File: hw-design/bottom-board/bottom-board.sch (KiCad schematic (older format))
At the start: 0 parts

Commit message: bottom,sch: minor adjustments
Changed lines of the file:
@@
 F1 "connectors.sch" 60
 $EndSheet
-Text Notes 1350 5600 0    80   ~ 0
+Text Notes 1350 6000 0    80   ~ 0
 - All resistors named as RA* must have 1% tolerance\n- All non-polarized capacitors named as CA* must use NP0 Temp. Coef.\n- All other non-polarized capacitors should use X7R Temp. Coef.\n- Decoupling caps must be placed as close as possible of the IC power pins
-Text Notes 1300 5000 0    100  ~ 20
+Text Notes 1300 5400 0    100  ~ 20
 Notes\n
 Wire Notes Line
-	1200 5000 1200 6200
+	1200 5400 1200 6600
 Wire Notes Line
-	1200 6200 6850 6200
+	1200 6600 6850 6600
 Wire Notes Line
-	6850 6200 6850 4800
+	6850 6600 6850 5200
 Wire Notes Line
-	6850 4800 1200 4800
+	6850 5200 1200 5200
 Wire Notes Line
-	1200 4800 1200 5050
+	1200 5200 1200 5450
 Wire Notes Line
-	1200 5050 6850 5050
+	1200 5450 6850 5450
 $Sheet
 S 1300 2250 2150 400

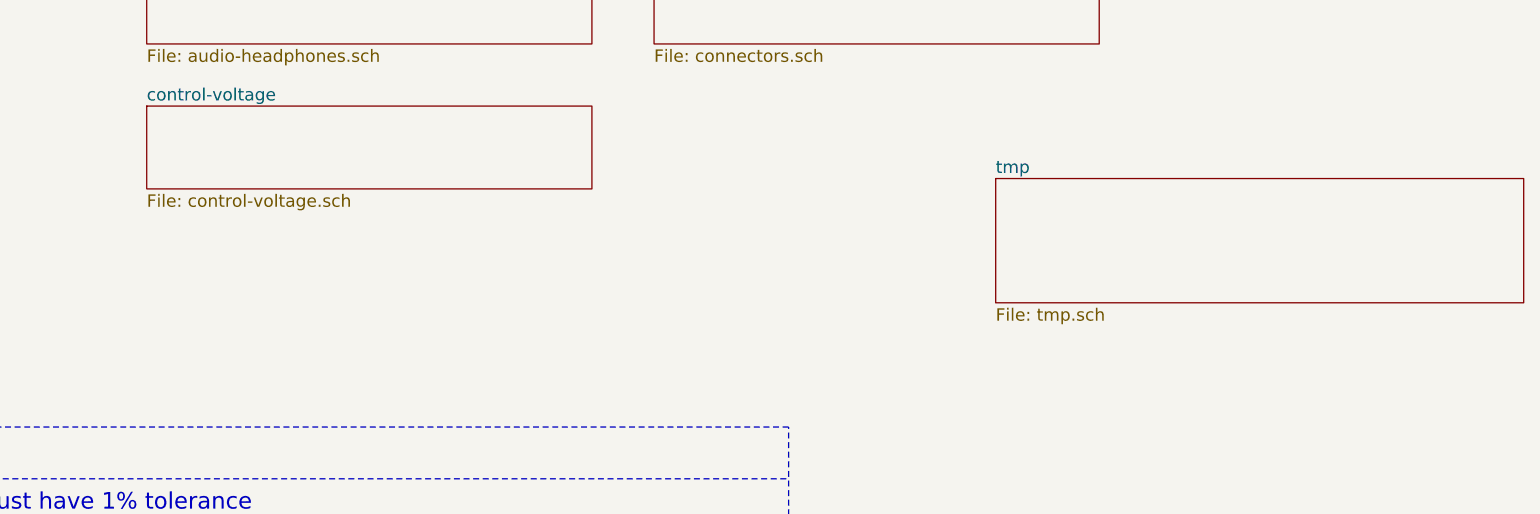
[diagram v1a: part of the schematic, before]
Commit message: bottom,sch: initial spdif circuit
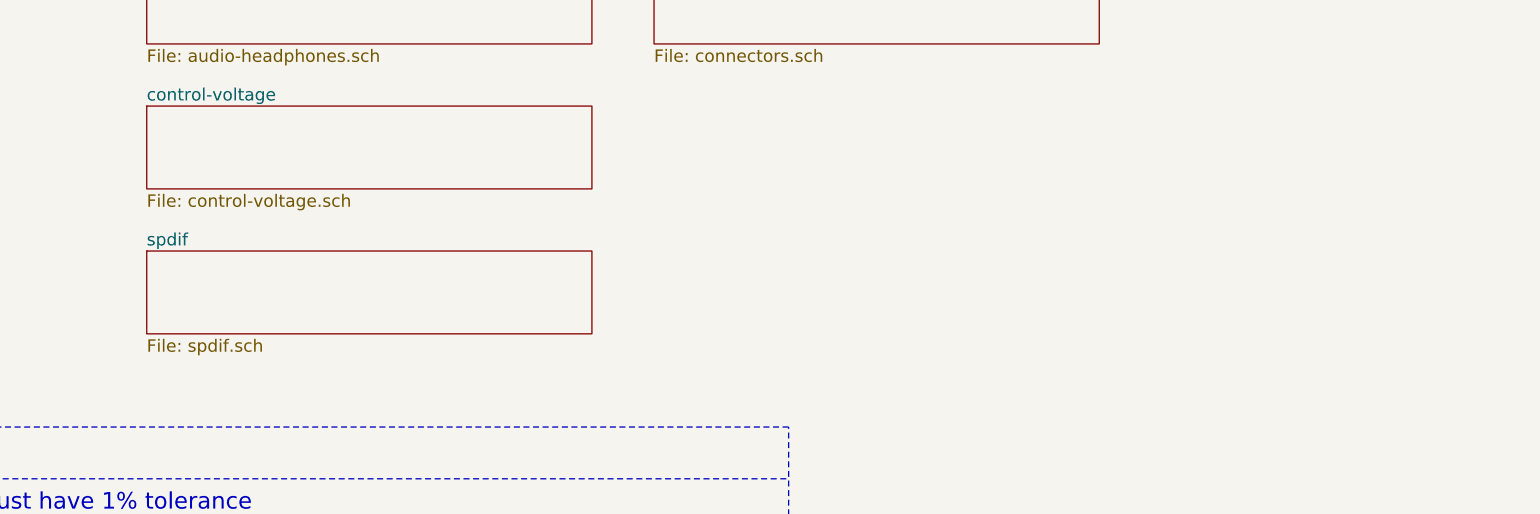
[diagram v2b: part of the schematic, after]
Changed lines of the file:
@@
 LIBS:74xx
 LIBS:Oscillators
+LIBS:transf
 LIBS:bottom-board-cache
 EELAYER 25 0
@@
 $EndSheet
 $Sheet
-S 7850 4000 2550 600
-U 5B52A3DA
-F0 "tmp" 60
-F1 "tmp.sch" 60
+S 3750 4350 2150 400
+U 5B6E0697
+F0 "spdif" 60
+F1 "spdif.sch" 60
 $EndSheet
 $EndSCHEMATC

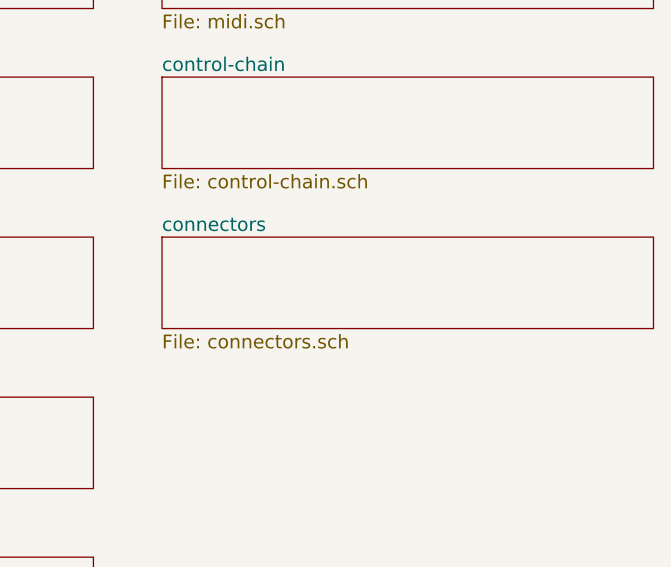
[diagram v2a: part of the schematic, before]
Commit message: bottom,sch: move hmi data connector to coreboard sheet
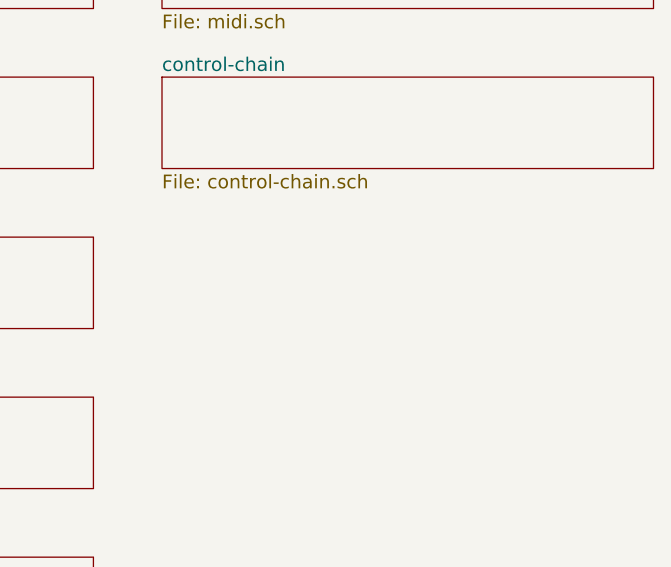
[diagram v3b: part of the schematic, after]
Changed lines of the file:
@@
 F1 "control-chain.sch" 60
-$EndSheet
-$Sheet
-S 6200 2950 2150 400
-U 54F72FB8
-F0 "connectors" 60
-F1 "connectors.sch" 60
 $EndSheet
 Text Notes 1350 6000 0    80   ~ 0

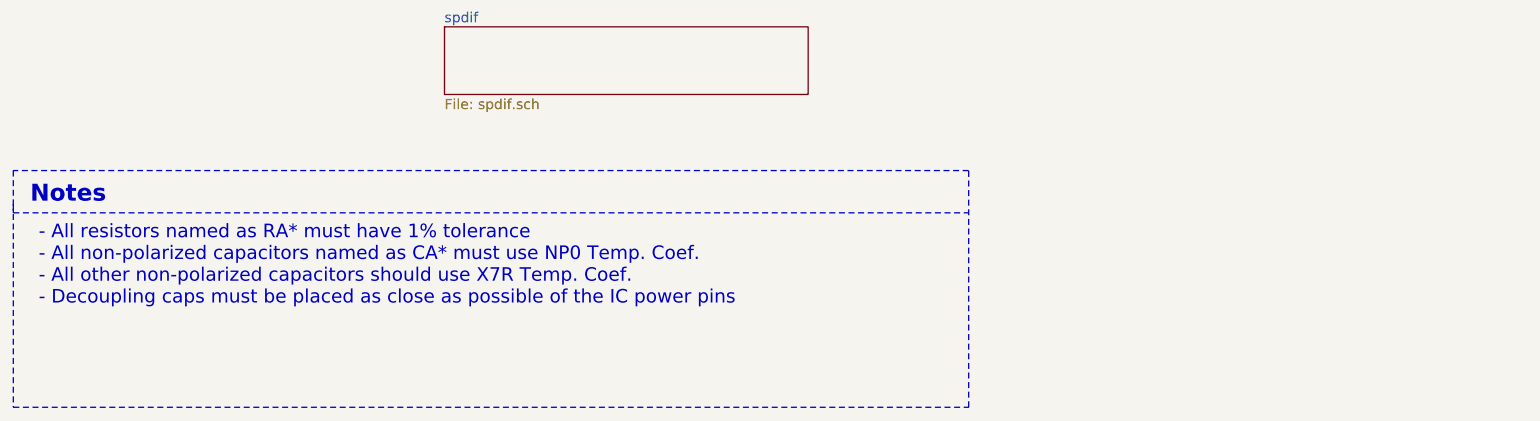
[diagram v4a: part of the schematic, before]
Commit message: bottom,sch: fix parts after updating to kicad 5
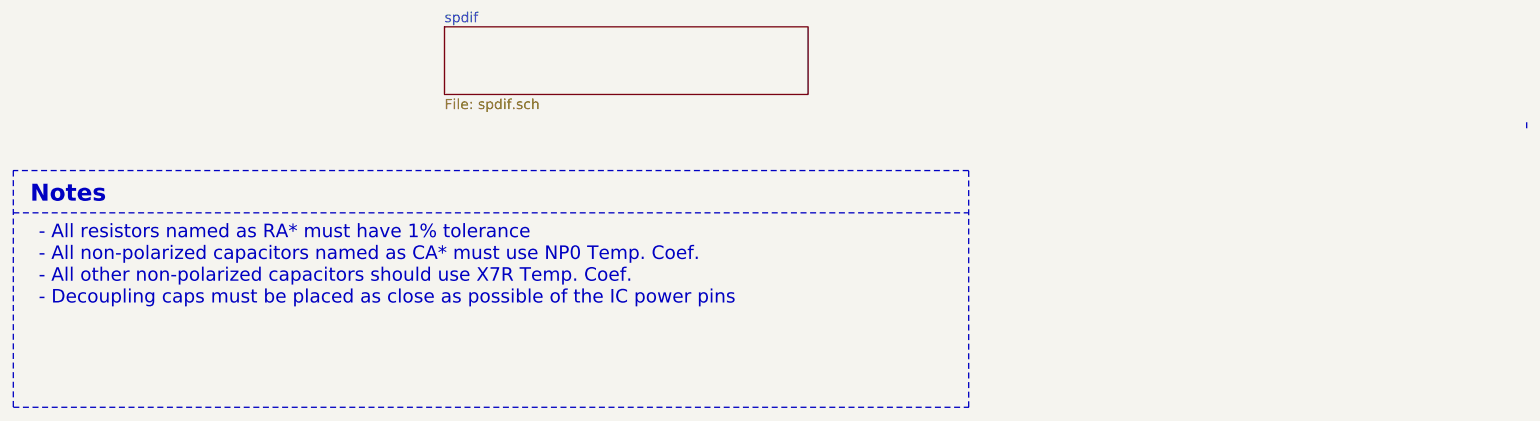
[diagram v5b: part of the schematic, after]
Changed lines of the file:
@@
-EESchema Schematic File Version 2
-LIBS:bottom-board-rescue
-LIBS:local-components
-LIBS:conn
-LIBS:device
-LIBS:digital-audio
-LIBS:interface
-LIBS:linear
-LIBS:opto
-LIBS:power
-LIBS:regul
-LIBS:relays
-LIBS:switches
-LIBS:ESD_Protection
-LIBS:Power_Management
-LIBS:memory
-LIBS:itead
-LIBS:adc-dac
-LIBS:analog_switches
-LIBS:battery_management
-LIBS:74xgxx
-LIBS:74xx
-LIBS:Oscillators
-LIBS:transf
+EESchema Schematic File Version 4
 LIBS:bottom-board-cache
-EELAYER 25 0
+EELAYER 26 0
 EELAYER END
 $Descr A4 11693 8268
@@
 Notes\n
 Wire Notes Line
-	1200 5400 1200 6600
-Wire Notes Line
 	1200 6600 6850 6600
 Wire Notes Line
@@
 Wire Notes Line
 	6850 5200 1200 5200
-Wire Notes Line
-	1200 5200 1200 5450
 Wire Notes Line
 	1200 5450 6850 5450
@@
 F1 "spdif.sch" 60
 $EndSheet
+Wire Notes Line
+	1200 5200 1200 6600
+Wire Notes Line
+	10150 4950 10150 4900
 $EndSCHEMATC

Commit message: bottom,sch: many fixes and addition of test points
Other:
- note added: "- All resistors named as RA* must have at least 1% tolerance\n- All non-polarized capacitors named as CA* must use NP0 Temp. Coef.\n- All other non-polarized capacitors should use X7R Temp. Coef.\n- Decoupling caps must be placed as close as possible of the IC power pins"
- note removed: "- All resistors named as RA* must have 1% tolerance\n- All non-polarized capacitors named as CA* must use NP0 Temp. Coef.\n- All other non-polarized capacitors should use X7R Temp. Coef.\n- Decoupling caps must be placed as close as possible of the IC power pins"
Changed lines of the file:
@@
 $EndSheet
 Text Notes 1350 6000 0    80   ~ 0
-- All resistors named as RA* must have 1% tolerance\n- All non-polarized capacitors named as CA* must use NP0 Temp. Coef.\n- All other non-polarized capacitors should use X7R Temp. Coef.\n- Decoupling caps must be placed as close as possible of the IC power pins
+- All resistors named as RA* must have at least 1% tolerance\n- All non-polarized capacitors named as CA* must use NP0 Temp. Coef.\n- All other non-polarized capacitors should use X7R Temp. Coef.\n- Decoupling caps must be placed as close as possible of the IC power pins
 Text Notes 1300 5400 0    100  ~ 20
 Notes\n
